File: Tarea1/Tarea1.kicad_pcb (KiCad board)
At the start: 2 copper layers, 10 parts, among them J1 Conn_01x02_Socket, J2 Conn_01x02_Socket, U1 LM2596T-ADJ

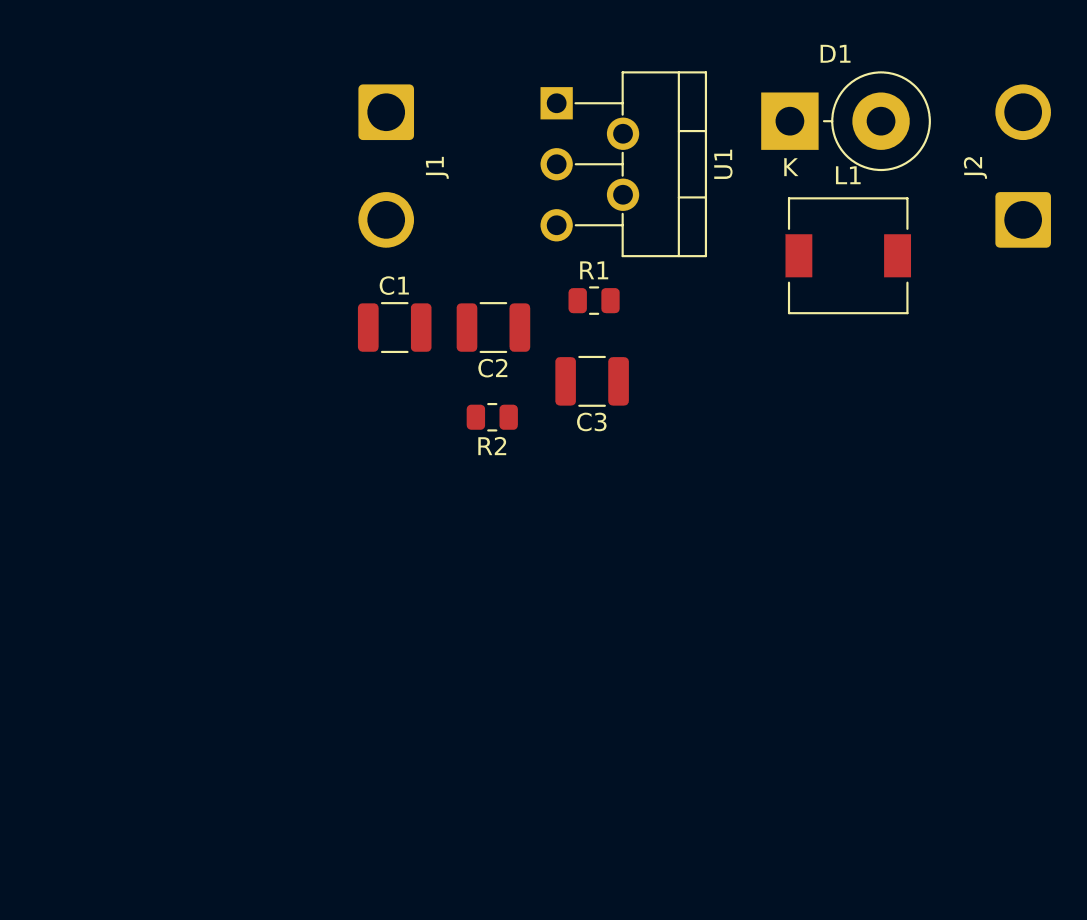
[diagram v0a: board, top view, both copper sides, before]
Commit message: Diseño de PCB sobre un conversor reductor
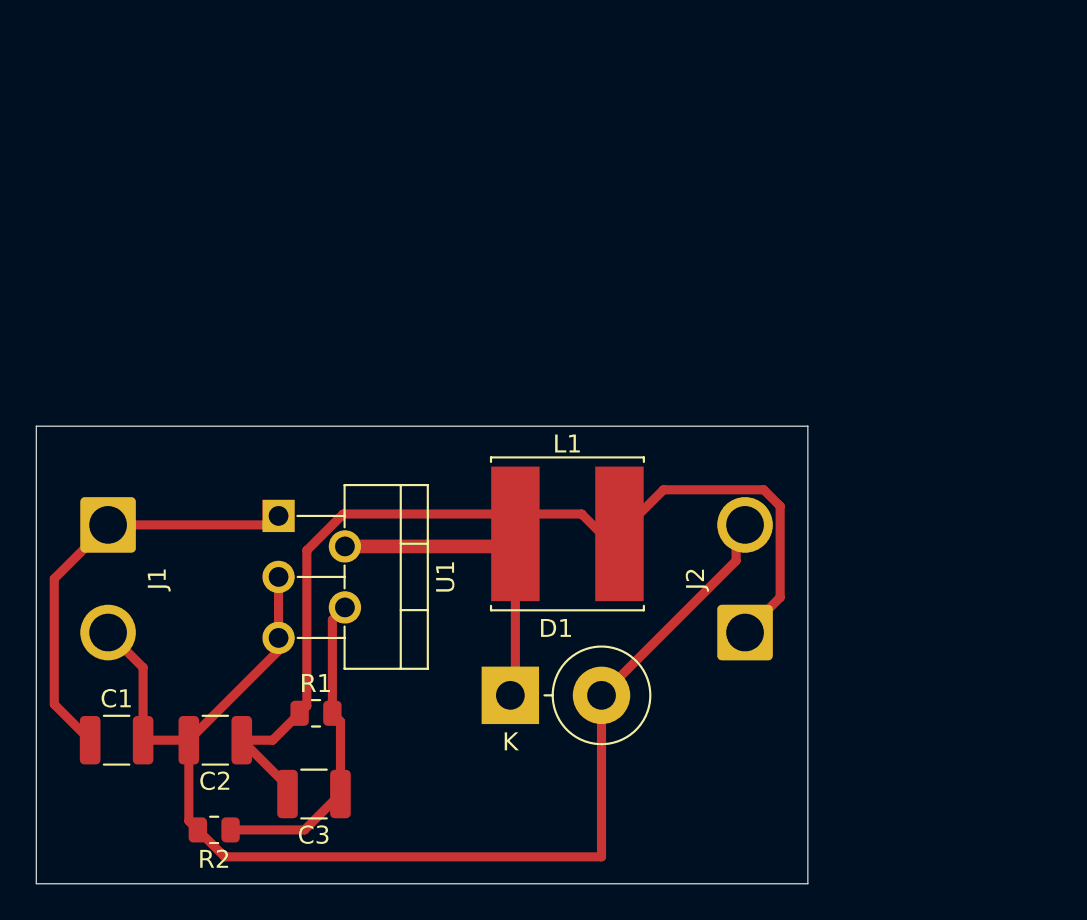
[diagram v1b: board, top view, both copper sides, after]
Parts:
- C1: value C -> 100uF
- C2: value C -> 220uF
- J1: value Conn_01x02_Socket -> Vin
- J2: value Conn_01x02_Socket -> Vout
- L1: footprint Inductor_SMD:L_6.3x6.3_H3 -> Inductor_SMD:L_Cenker_CKCS8080
- R1: value R -> 3.1k
- R2: value R -> 1k
- moved D1 35.6 mm to (111.4, 64.0)
- moved C1 27.7 mm to (89.5, 66.5)
- moved C2 27.7 mm to (95.0, 66.5)
- moved C3 27.7 mm to (100.5, 69.5)
- moved J1 27.7 mm to (89.0, 54.5)
- moved J2 27.7 mm to (124.5, 60.5)
- moved R1 27.7 mm to (100.6, 65.0)
- moved R2 27.7 mm to (94.9, 71.5)
- moved U1 27.7 mm to (98.5, 54.0)
- moved L1 22.0 mm to (114.6, 55.0)
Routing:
- net GND: track 0.00 -> 70.7 mm
- net Net-(J2-Pin_1): track 0.00 -> 54.8 mm
- net Net-(J1-Pin_1): track 0.00 -> 23.8 mm
- net Net-(D1-K): track 0.00 -> 20.0 mm
- net Net-(U1-FB): track 0.00 -> 17.8 mm
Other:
- board outline added: 43 x 25.5 mm
- board text added: "Step Down Voltage Converter"
- board text added: "Vin"
- board text added: "Vout"
